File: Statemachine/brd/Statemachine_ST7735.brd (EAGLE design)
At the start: 100 x 80 mm, 11 parts

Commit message: board routed
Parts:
- moved S3 2.84 mm to (10.2, 50.8)
- moved S1 1.80 mm to (10.2, 25.4)
- moved JP2 1.27 mm to (94.0, 16.5)
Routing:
- net BTN1: track 5.08 -> 144.8 mm, vias 0 -> 4
- net BTN2: track 10.2 -> 96.5 mm, vias 0 -> 4
- net GND: track 188.0 -> 223.5 mm, vias 7 -> 9
- net +5V: track 127.0 -> 152.4 mm, vias 6 -> 8
- net SCL: track 109.2 -> 119.4 mm, vias 1 -> 3
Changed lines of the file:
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@@
 <?xml version="1.0" encoding="utf-8"?>
 <!DOCTYPE eagle SYSTEM "eagle.dtd">
-<eagle version="6.5.0">
+<eagle version="6.4">
 <drawing>
 <settings>
@@
 <element name="U$1" library="arduino" package="PDIP-32" value="ARDUINONANO" x="63.5" y="58.42"/>
 <element name="JP1" library="pinhead" package="1X04" value="SHT11" x="93.98" y="57.15" rot="R90"/>
-<element name="JP2" library="pinhead" package="1X02" value="Power" x="93.98" y="15.24" rot="R270"/>
+<element name="JP2" library="pinhead" package="1X02" value="Power" x="93.98" y="16.51" rot="R270"/>
 <element name="R1" library="resistor" package="0207/10" value="10k" x="88.9" y="33.02" rot="R90"/>
 <element name="R2" library="resistor" package="0204/7" value="10k" x="83.82" y="34.29" rot="R90"/>
@@
 <element name="R3" library="resistor" package="0204/7" value="10k" x="53.34" y="62.23" rot="R90"/>
 <element name="R4" library="resistor" package="0207/10" value="10k" x="58.42" y="60.96" rot="R90"/>
-<element name="S3" library="switch-misc" package="DT6" value="DT6" x="8.89" y="48.26" rot="R180"/>
-<element name="S1" library="switch-misc" package="DT6" value="DT6" x="8.89" y="26.67" rot="R180"/>
+<element name="S3" library="switch-misc" package="DT6" value="DT6" x="10.16" y="50.8" rot="R180"/>
+<element name="S1" library="switch-misc" package="DT6" value="DT6" x="10.16" y="25.4" rot="R180"/>
 </elements>
 <signals>
@@
 <via x="20.32" y="66.04" extent="1-16" drill="0.6" shape="square"/>
 <wire x1="86.36" y1="38.1" x2="88.9" y2="38.1" width="0" layer="19" extent="16-16"/>
-<wire x1="93.98" y1="16.51" x2="93.98" y2="38.1" width="0" layer="19" extent="1-1"/>
+<wire x1="93.98" y1="38.1" x2="96.52" y2="38.1" width="0.4064" layer="16"/>
+<wire x1="96.52" y1="38.1" x2="96.52" y2="17.78" width="0.4064" layer="1"/>
+<wire x1="96.52" y1="17.78" x2="93.98" y2="17.78" width="0.4064" layer="16"/>
+<via x="96.52" y="38.1" extent="1-16" drill="0.6" shape="square"/>
+<via x="96.52" y="17.78" extent="1-16" drill="0.6" shape="square"/>
 </signal>
 <signal name="GND">
@@
 <contactref element="S3" pad="3"/>
 <contactref element="S1" pad="3"/>
-<wire x1="22.86" y1="68.58" x2="6.35" y2="68.58" width="0.4064" layer="16"/>
-<wire x1="6.35" y1="68.58" x2="6.35" y2="50.8" width="0" layer="19" extent="1-16"/>
-<wire x1="22.86" y1="60.96" x2="22.86" y2="68.58" width="0.4064" layer="1"/>
-<wire x1="22.86" y1="68.58" x2="93.98" y2="68.58" width="0.4064" layer="16"/>
-<wire x1="93.98" y1="68.58" x2="93.98" y2="60.96" width="0.4064" layer="1"/>
-<wire x1="97.79" y1="40.64" x2="97.79" y2="60.96" width="0.4064" layer="1"/>
-<wire x1="97.79" y1="60.96" x2="93.98" y2="60.96" width="0.4064" layer="16"/>
-<wire x1="63.5" y1="48.26" x2="22.86" y2="48.26" width="0.4064" layer="16"/>
+<wire x1="96.52" y1="40.64" x2="96.52" y2="60.96" width="0.4064" layer="1"/>
+<wire x1="96.52" y1="60.96" x2="93.98" y2="60.96" width="0.4064" layer="16"/>
+<wire x1="63.5" y1="48.26" x2="38.1" y2="48.26" width="0.4064" layer="16"/>
 <wire x1="22.86" y1="48.26" x2="22.86" y2="60.96" width="0.4064" layer="1"/>
-<wire x1="93.98" y1="40.64" x2="97.79" y2="40.64" width="0.4064" layer="16"/>
-<wire x1="97.79" y1="13.97" x2="93.98" y2="13.97" width="0.4064" layer="16"/>
+<wire x1="93.98" y1="40.64" x2="96.52" y2="40.64" width="0.4064" layer="16"/>
 <via x="22.86" y="48.26" extent="1-16" drill="0.6" shape="square"/>
-<via x="93.98" y="68.58" extent="1-16" drill="0.6" shape="square"/>
-<via x="97.79" y="40.64" extent="1-16" drill="0.6" shape="square"/>
-<via x="97.79" y="60.96" extent="1-16" drill="0.6" shape="square"/>
-<via x="97.79" y="13.97" extent="1-16" drill="0.6" shape="square"/>
-<via x="6.35" y="68.58" extent="1-16" drill="0.6" shape="square"/>
-<via x="22.86" y="68.58" extent="1-16" drill="0.6" shape="square"/>
-<wire x1="93.98" y1="40.64" x2="93.98" y2="13.97" width="0" layer="19" extent="1-1"/>
-<wire x1="6.35" y1="29.21" x2="6.35" y2="50.8" width="0" layer="19" extent="1-1"/>
+<via x="96.52" y="40.64" extent="1-16" drill="0.6" shape="square"/>
+<via x="96.52" y="60.96" extent="1-16" drill="0.6" shape="square"/>
+<wire x1="7.62" y1="27.94" x2="20.32" y2="27.94" width="0.4064" layer="16"/>
+<wire x1="20.32" y1="27.94" x2="20.32" y2="48.26" width="0.4064" layer="1"/>
+<wire x1="20.32" y1="48.26" x2="22.86" y2="48.26" width="0.4064" layer="16"/>
+<wire x1="22.86" y1="48.26" x2="38.1" y2="48.26" width="0.4064" layer="16"/>
+<wire x1="38.1" y1="48.26" x2="38.1" y2="53.34" width="0.4064" layer="1"/>
+<wire x1="38.1" y1="53.34" x2="7.62" y2="53.34" width="0.4064" layer="16"/>
+<via x="38.1" y="48.26" extent="1-16" drill="0.6" shape="square"/>
+<via x="38.1" y="53.34" extent="1-16" drill="0.6" shape="square"/>
+<via x="20.32" y="27.94" extent="1-16" drill="0.6" shape="square"/>
+<via x="20.32" y="48.26" extent="1-16" drill="0.6" shape="square"/>
+<wire x1="63.5" y1="48.26" x2="68.58" y2="48.26" width="0.4064" layer="16"/>
+<wire x1="68.58" y1="48.26" x2="68.58" y2="60.96" width="0.4064" layer="16"/>
+<wire x1="68.58" y1="60.96" x2="93.98" y2="60.96" width="0.4064" layer="16"/>
+<wire x1="93.98" y1="15.24" x2="91.44" y2="15.24" width="0.4064" layer="16"/>
+<wire x1="91.44" y1="15.24" x2="91.44" y2="40.64" width="0.4064" layer="1"/>
+<wire x1="91.44" y1="40.64" x2="93.98" y2="40.64" width="0.4064" layer="16"/>
+<via x="91.44" y="15.24" extent="1-16" drill="0.6" shape="square"/>
+<via x="91.44" y="40.64" extent="1-16" drill="0.6" shape="square"/>
 </signal>
 <signal name="BTN1">
@@
 <contactref element="S3" pad="1"/>
 <wire x1="78.74" y1="30.48" x2="83.82" y2="30.48" width="0.4064" layer="16"/>
-<wire x1="11.43" y1="45.72" x2="78.74" y2="30.48" width="0" layer="19" extent="1-1"/>
+<wire x1="78.74" y1="30.48" x2="86.36" y2="30.48" width="0.4064" layer="16"/>
+<wire x1="86.36" y1="30.48" x2="86.36" y2="10.16" width="0.4064" layer="1"/>
+<wire x1="86.36" y1="10.16" x2="17.78" y2="10.16" width="0.4064" layer="16"/>
+<wire x1="17.78" y1="10.16" x2="17.78" y2="48.26" width="0.4064" layer="1"/>
+<wire x1="17.78" y1="48.26" x2="12.7" y2="48.26" width="0.4064" layer="16"/>
+<via x="17.78" y="10.16" extent="1-16" drill="0.6" shape="square"/>
+<via x="17.78" y="48.26" extent="1-16" drill="0.6" shape="square"/>
+<via x="86.36" y="30.48" extent="1-16" drill="0.6" shape="square"/>
+<via x="86.36" y="10.16" extent="1-16" drill="0.6" shape="square"/>
 </signal>
 <signal name="BTN2">
@@
 <contactref element="S1" pad="1"/>
 <wire x1="88.9" y1="27.94" x2="78.74" y2="27.94" width="0.4064" layer="16"/>
-<wire x1="11.43" y1="24.13" x2="78.74" y2="27.94" width="0" layer="19" extent="1-1"/>
+<wire x1="78.74" y1="27.94" x2="73.66" y2="27.94" width="0.4064" layer="16"/>
+<wire x1="73.66" y1="27.94" x2="73.66" y2="15.24" width="0.4064" layer="1"/>
+<wire x1="73.66" y1="15.24" x2="20.32" y2="15.24" width="0.4064" layer="16"/>
+<wire x1="20.32" y1="15.24" x2="20.32" y2="22.86" width="0.4064" layer="1"/>
+<wire x1="20.32" y1="22.86" x2="12.7" y2="22.86" width="0.4064" layer="16"/>
+<via x="73.66" y="27.94" extent="1-16" drill="0.6" shape="square"/>
+<via x="73.66" y="15.24" extent="1-16" drill="0.6" shape="square"/>
+<via x="20.32" y="15.24" extent="1-16" drill="0.6" shape="square"/>
+<via x="20.32" y="22.86" extent="1-16" drill="0.6" shape="square"/>
 </signal>
 <signal name="+3V3">
@@
 <wire x1="25.4" y1="12.7" x2="25.4" y2="60.96" width="0.4064" layer="1"/>
 <via x="25.4" y="12.7" extent="1-16" drill="0.6" shape="square"/>
-<wire x1="78.74" y1="20.32" x2="76.2" y2="20.32" width="0.4064" layer="16"/>
-<wire x1="76.2" y1="20.32" x2="76.2" y2="12.7" width="0.4064" layer="16"/>
-<wire x1="76.2" y1="12.7" x2="25.4" y2="12.7" width="0.4064" layer="16"/>
+<wire x1="78.74" y1="20.32" x2="83.82" y2="20.32" width="0.4064" layer="16"/>
+<wire x1="83.82" y1="20.32" x2="83.82" y2="12.7" width="0.4064" layer="1"/>
+<wire x1="83.82" y1="12.7" x2="25.4" y2="12.7" width="0.4064" layer="16"/>
+<via x="83.82" y="20.32" extent="1-16" drill="0.6" shape="square"/>
+<via x="83.82" y="12.7" extent="1-16" drill="0.6" shape="square"/>
 </signal>
 <signal name="SDA">

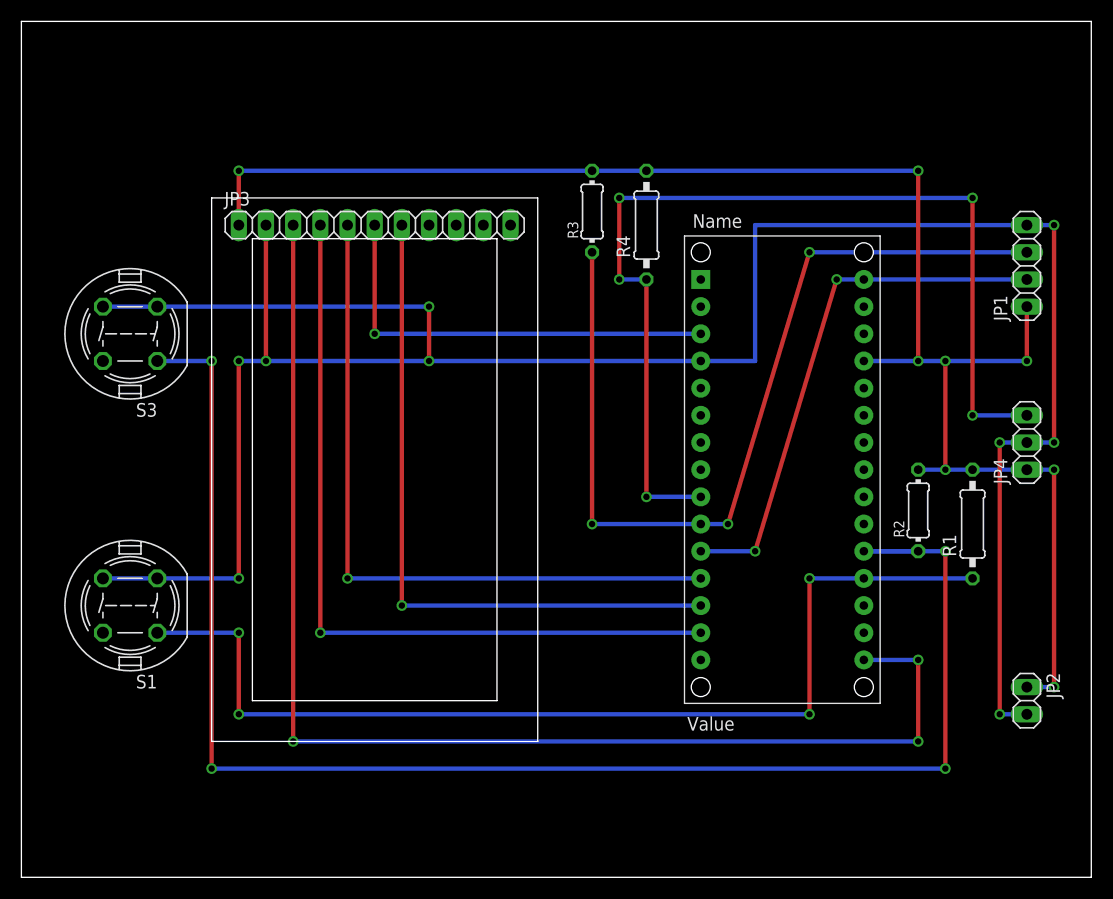
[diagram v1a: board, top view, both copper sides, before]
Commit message: add sd card
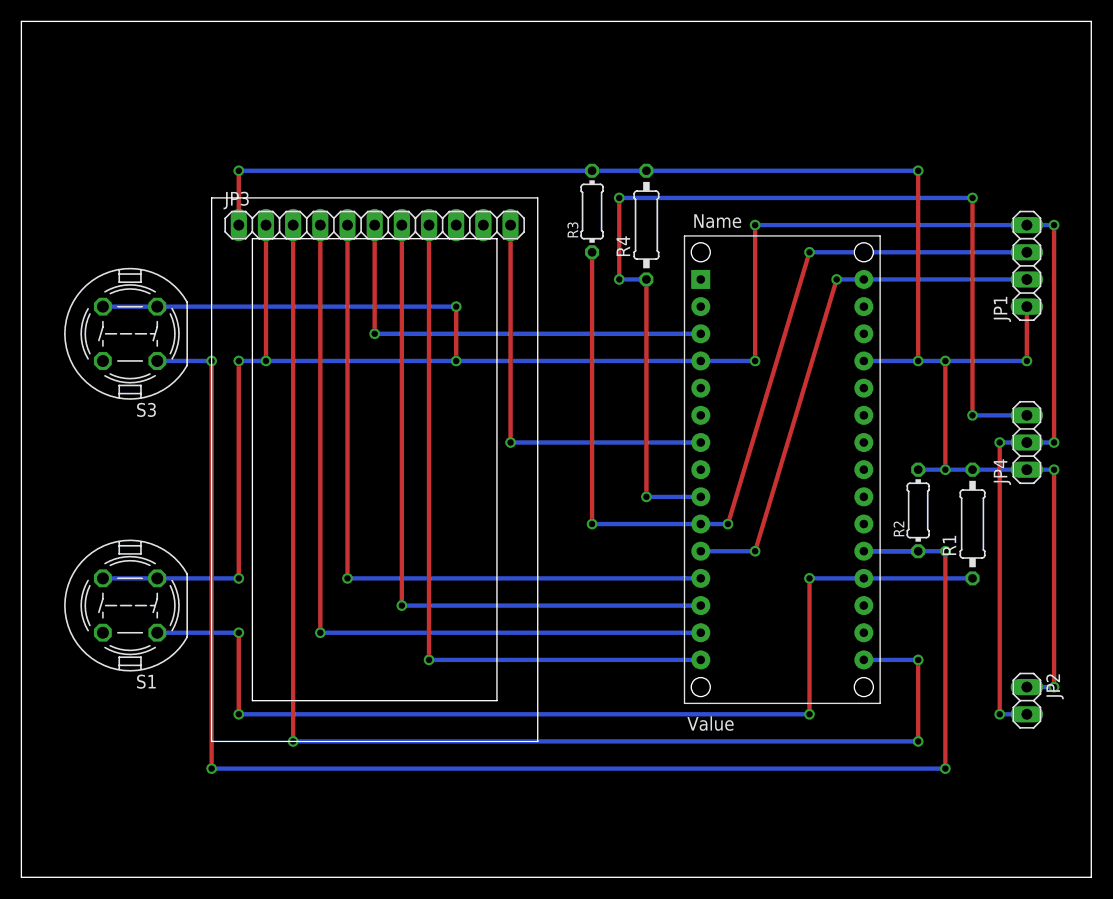
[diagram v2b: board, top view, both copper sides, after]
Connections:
- removed net MOSI: JP3.10
- removed net SCLK: JP3.9
- net CS-SD: now also U$1.D4
- net MISO: now also U$1.D12
- net SCL: now also JP3.9
- net SDA: now also JP3.10
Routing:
- net MISO: track 0.00 -> 66.0 mm, vias 0 -> 1
- net CS-SD: track 0.00 -> 38.1 mm, vias 0 -> 1
- net GND: track 223.5 -> 226.1 mm, vias 9 -> 11
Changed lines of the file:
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@@
 <wire x1="96.52" y1="40.64" x2="96.52" y2="60.96" width="0.4064" layer="1"/>
 <wire x1="96.52" y1="60.96" x2="93.98" y2="60.96" width="0.4064" layer="16"/>
-<wire x1="63.5" y1="48.26" x2="38.1" y2="48.26" width="0.4064" layer="16"/>
+<wire x1="63.5" y1="48.26" x2="40.64" y2="48.26" width="0.4064" layer="16"/>
 <wire x1="22.86" y1="48.26" x2="22.86" y2="60.96" width="0.4064" layer="1"/>
 <wire x1="93.98" y1="40.64" x2="96.52" y2="40.64" width="0.4064" layer="16"/>
@@
 <wire x1="20.32" y1="27.94" x2="20.32" y2="48.26" width="0.4064" layer="1"/>
 <wire x1="20.32" y1="48.26" x2="22.86" y2="48.26" width="0.4064" layer="16"/>
-<wire x1="22.86" y1="48.26" x2="38.1" y2="48.26" width="0.4064" layer="16"/>
-<wire x1="38.1" y1="48.26" x2="38.1" y2="53.34" width="0.4064" layer="1"/>
-<wire x1="38.1" y1="53.34" x2="7.62" y2="53.34" width="0.4064" layer="16"/>
-<via x="38.1" y="48.26" extent="1-16" drill="0.6" shape="square"/>
-<via x="38.1" y="53.34" extent="1-16" drill="0.6" shape="square"/>
+<wire x1="22.86" y1="48.26" x2="40.64" y2="48.26" width="0.4064" layer="16"/>
+<wire x1="40.64" y1="48.26" x2="40.64" y2="53.34" width="0.4064" layer="1"/>
+<wire x1="40.64" y1="53.34" x2="7.62" y2="53.34" width="0.4064" layer="16"/>
+<via x="40.64" y="48.26" extent="1-16" drill="0.6" shape="square"/>
+<via x="40.64" y="53.34" extent="1-16" drill="0.6" shape="square"/>
 <via x="20.32" y="27.94" extent="1-16" drill="0.6" shape="square"/>
 <via x="20.32" y="48.26" extent="1-16" drill="0.6" shape="square"/>
 <wire x1="63.5" y1="48.26" x2="68.58" y2="48.26" width="0.4064" layer="16"/>
-<wire x1="68.58" y1="48.26" x2="68.58" y2="60.96" width="0.4064" layer="16"/>
+<wire x1="68.58" y1="48.26" x2="68.58" y2="60.96" width="0.4064" layer="1"/>
 <wire x1="68.58" y1="60.96" x2="93.98" y2="60.96" width="0.4064" layer="16"/>
 <wire x1="93.98" y1="15.24" x2="91.44" y2="15.24" width="0.4064" layer="16"/>
@@
 <via x="91.44" y="15.24" extent="1-16" drill="0.6" shape="square"/>
 <via x="91.44" y="40.64" extent="1-16" drill="0.6" shape="square"/>
+<via x="68.58" y="48.26" extent="1-16" drill="0.6" shape="square"/>
+<via x="68.58" y="60.96" extent="1-16" drill="0.6" shape="square"/>
 </signal>
 <signal name="BTN1">
@@
 <via x="83.82" y="20.32" extent="1-16" drill="0.6" shape="square"/>
 <via x="83.82" y="12.7" extent="1-16" drill="0.6" shape="square"/>
+<contactref element="JP3" pad="9"/>
+<wire x1="25.4" y1="60.96" x2="40.64" y2="60.96" width="0" layer="19" extent="1-1"/>
 </signal>
 <signal name="SDA">
@@
 <wire x1="27.94" y1="22.86" x2="27.94" y2="60.96" width="0.4064" layer="1"/>
 <via x="27.94" y="22.86" extent="1-16" drill="0.6" shape="square"/>
+<contactref element="JP3" pad="10"/>
+<wire x1="27.94" y1="60.96" x2="43.18" y2="60.96" width="0" layer="19" extent="1-1"/>
 </signal>
 <signal name="CS-LCD">
@@
 <signal name="MISO">
 <contactref element="JP3" pad="8"/>
-</signal>
-<signal name="SCLK">
-<contactref element="JP3" pad="9"/>
-</signal>
-<signal name="MOSI">
-<contactref element="JP3" pad="10"/>
+<contactref element="U$1" pad="D12"/>
+<wire x1="63.5" y1="20.32" x2="38.1" y2="20.32" width="0.4064" layer="16"/>
+<via x="38.1" y="20.32" extent="1-16" drill="0.6" shape="square"/>
+<wire x1="38.1" y1="20.32" x2="38.1" y2="60.96" width="0.4064" layer="1"/>
 </signal>
 <signal name="CS-SD">
 <contactref element="JP3" pad="11"/>
+<contactref element="U$1" pad="D4"/>
+<wire x1="63.5" y1="40.64" x2="45.72" y2="40.64" width="0.4064" layer="16"/>
+<via x="45.72" y="40.64" extent="1-16" drill="0.6" shape="square"/>
+<wire x1="45.72" y1="40.64" x2="45.72" y2="60.96" width="0.4064" layer="1"/>
 </signal>
 <signal name="SHT-SCLK">

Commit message: add board
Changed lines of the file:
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@@
 <?xml version="1.0" encoding="utf-8"?>
 <!DOCTYPE eagle SYSTEM "eagle.dtd">
-<eagle version="6.4">
+<eagle version="6.5.0">
 <drawing>
 <settings>
@@
 <layer number="43" name="vRestrict" color="2" fill="10" visible="yes" active="yes"/>
 <layer number="44" name="Drills" color="7" fill="1" visible="no" active="yes"/>
-<layer number="45" name="Holes" color="7" fill="1" visible="no" active="yes"/>
+<layer number="45" name="Holes" color="7" fill="1" visible="yes" active="yes"/>
 <layer number="46" name="Milling" color="3" fill="1" visible="no" active="yes"/>
 <layer number="47" name="Measures" color="7" fill="1" visible="no" active="yes"/>
@@
 <wire x1="0" y1="80" x2="0" y2="0" width="0" layer="20"/>
 <frame x1="17.78" y1="12.7" x2="48.26" y2="63.5" columns="8" rows="5" layer="20" border-left="no" border-top="no" border-right="no" border-bottom="no"/>
+<hole x="81.28" y="38.1" drill="0.6"/>
+<hole x="81.28" y="40.64" drill="0.6"/>
+<hole x="81.28" y="43.18" drill="0.6"/>
+<hole x="81.28" y="53.34" drill="0.6"/>
+<hole x="71.12" y="55.88" drill="0.6"/>
+<hole x="71.12" y="53.34" drill="0.6"/>
+<hole x="71.12" y="50.8" drill="0.6"/>
+<hole x="71.12" y="48.26" drill="0.6"/>
+<hole x="71.12" y="45.72" drill="0.6"/>
+<hole x="71.12" y="43.18" drill="0.6"/>
+<hole x="71.12" y="40.64" drill="0.6"/>
+<hole x="71.12" y="38.1" drill="0.6"/>
+<hole x="71.12" y="35.56" drill="0.6"/>
+<hole x="71.12" y="33.02" drill="0.6"/>
+<hole x="71.12" y="30.48" drill="0.6"/>
+<hole x="71.12" y="27.94" drill="0.6"/>
+<hole x="71.12" y="25.4" drill="0.6"/>
+<hole x="71.12" y="22.86" drill="0.6"/>
+<hole x="71.12" y="20.32" drill="0.6"/>
+<hole x="88.9" y="15.24" drill="0.6"/>
+<hole x="22.86" y="22.86" drill="0.6"/>
+<hole x="22.86" y="27.94" drill="0.6"/>
+<hole x="60.96" y="53.34" drill="0.6"/>
+<hole x="17.78" y="48.26" drill="0.6"/>
+<hole x="71.12" y="58.42" drill="0.6"/>
+<hole x="66.04" y="60.96" drill="0.6"/>
 </plain>
 <attributes>
@@
 <wire x1="78.74" y1="30.48" x2="86.36" y2="30.48" width="0.4064" layer="16"/>
 <wire x1="86.36" y1="30.48" x2="86.36" y2="10.16" width="0.4064" layer="1"/>
-<wire x1="86.36" y1="10.16" x2="17.78" y2="10.16" width="0.4064" layer="16"/>
-<wire x1="17.78" y1="10.16" x2="17.78" y2="48.26" width="0.4064" layer="1"/>
-<wire x1="17.78" y1="48.26" x2="12.7" y2="48.26" width="0.4064" layer="16"/>
-<via x="17.78" y="10.16" extent="1-16" drill="0.6" shape="square"/>
-<via x="17.78" y="48.26" extent="1-16" drill="0.6" shape="square"/>
+<wire x1="86.36" y1="10.16" x2="15.24" y2="10.16" width="0.4064" layer="16"/>
+<wire x1="15.24" y1="10.16" x2="15.24" y2="48.26" width="0.4064" layer="1"/>
+<wire x1="15.24" y1="48.26" x2="12.7" y2="48.26" width="0.4064" layer="16"/>
+<via x="15.24" y="10.16" extent="1-16" drill="0.6" shape="square"/>
+<via x="15.24" y="48.26" extent="1-16" drill="0.6" shape="square"/>
 <via x="86.36" y="30.48" extent="1-16" drill="0.6" shape="square"/>
 <via x="86.36" y="10.16" extent="1-16" drill="0.6" shape="square"/>
